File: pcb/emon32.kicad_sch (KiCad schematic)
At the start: 37 parts

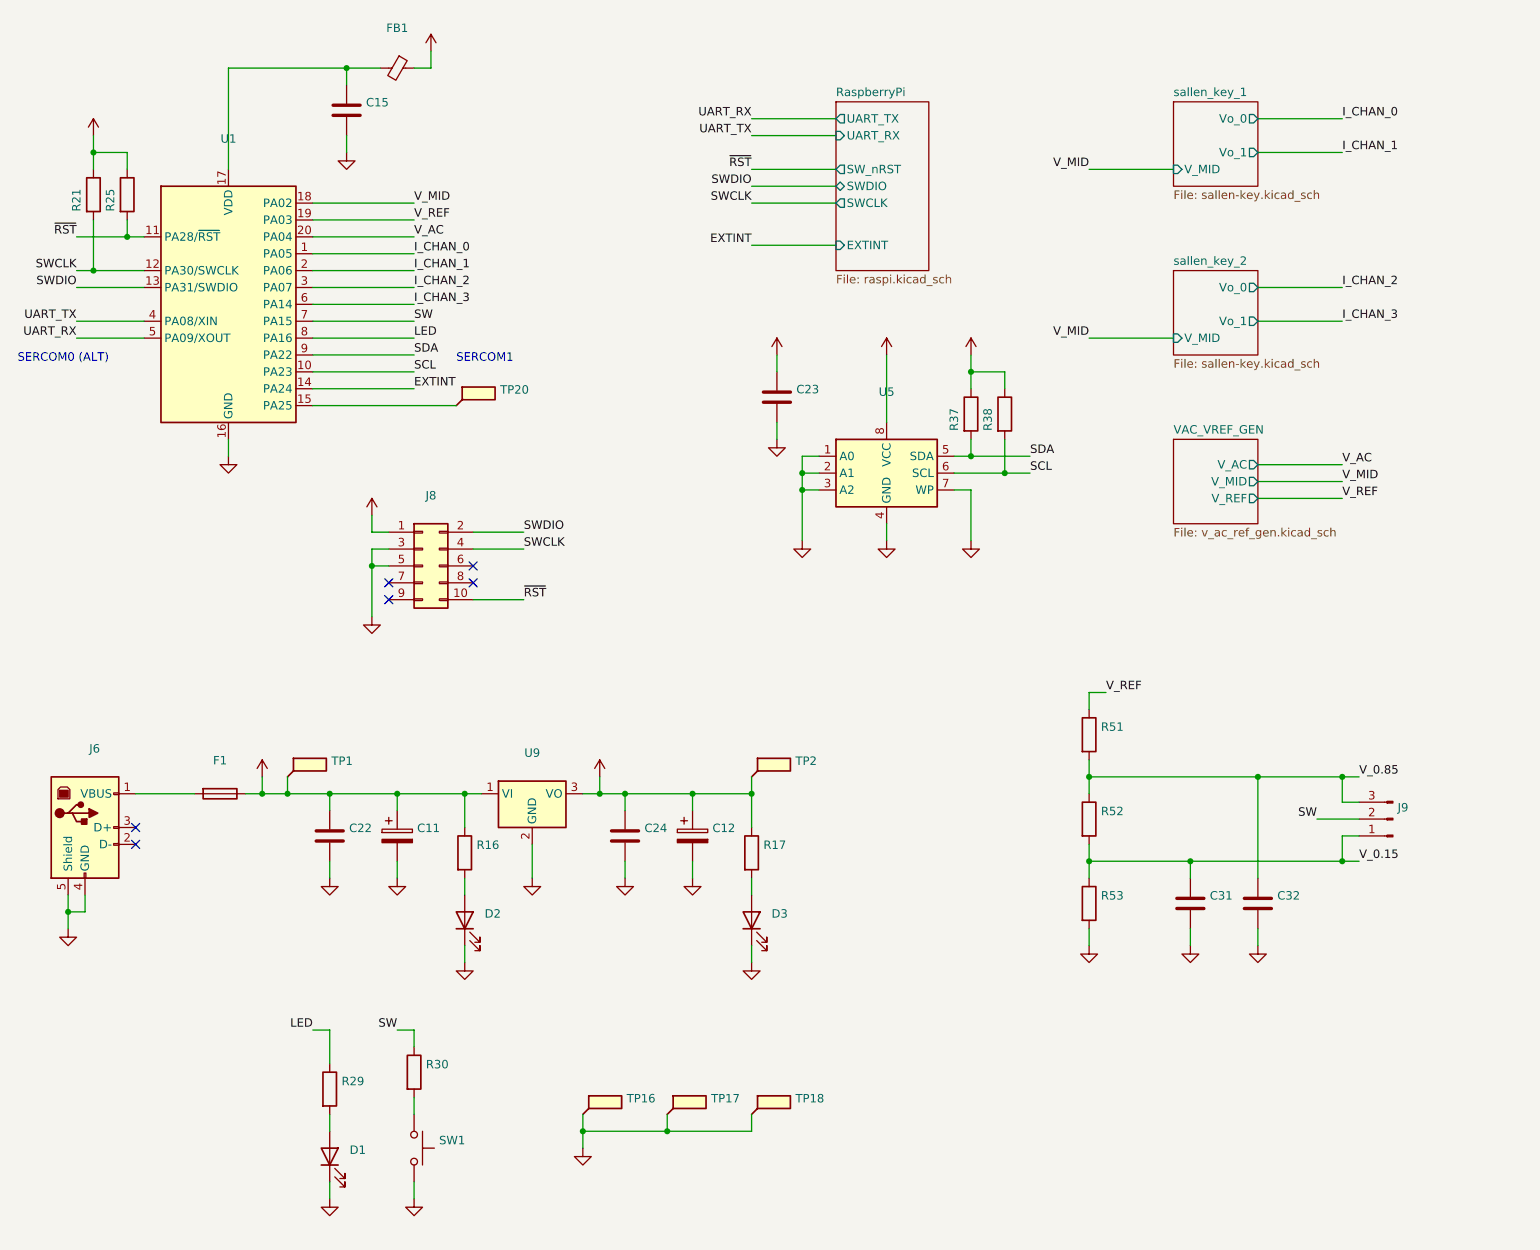
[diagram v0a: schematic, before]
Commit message: * Start replicating emonLibCM functionality
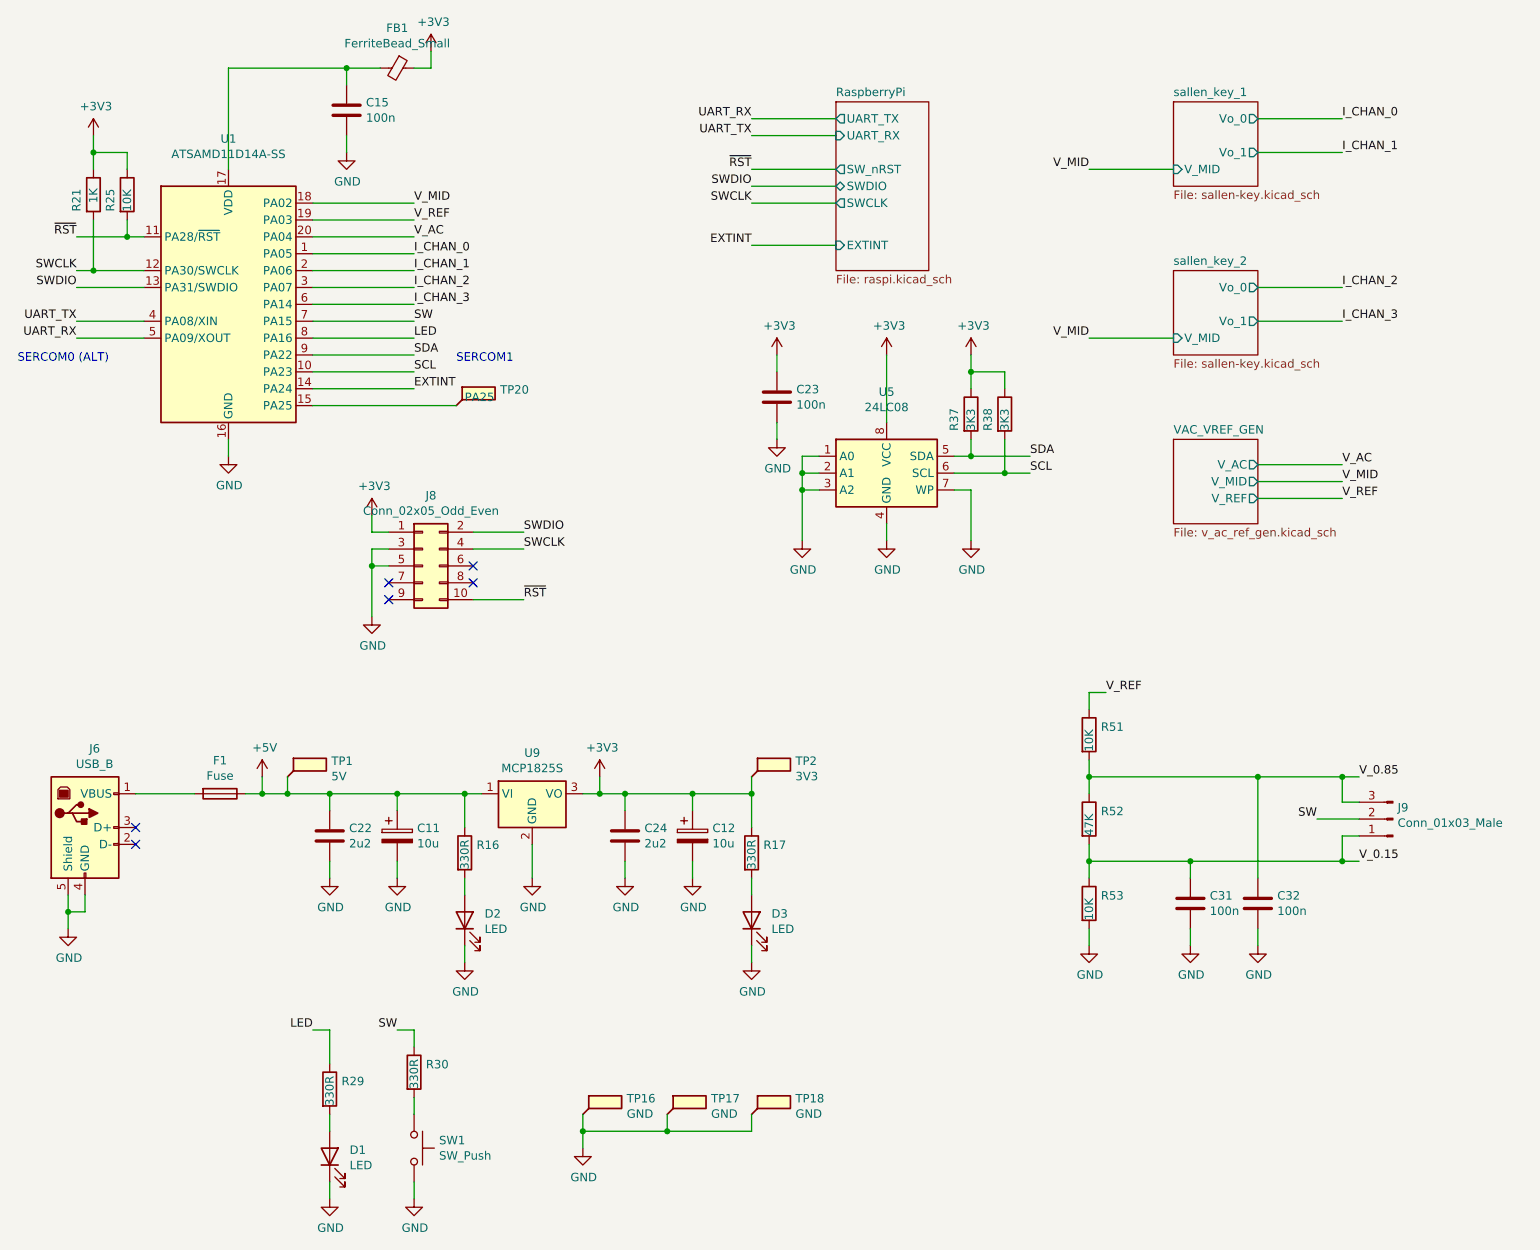
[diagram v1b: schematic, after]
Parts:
- C11, C12: value (none) -> 10u; footprint (none) -> Capacitor_THT:C_Radial_D6.3mm_H5.0mm_P2.50mm
- C15, C23, C31, C32: value (none) -> 100n; footprint (none) -> Capacitor_SMD:C_0805_2012Metric_Pad1.18x1.45mm_HandSolder
- C22, C24: value (none) -> 2u2; footprint (none) -> Capacitor_SMD:C_0805_2012Metric_Pad1.18x1.45mm_HandSolder
- D1, D2, D3: value (none) -> LED; footprint (none) -> LED_SMD:LED_0805_2012Metric_Pad1.15x1.40mm_HandSolder
- F1: value (none) -> Fuse; footprint (none) -> Fuse:Fuse_1206_3216Metric_Pad1.42x1.75mm_HandSolder
- FB1: value (none) -> FerriteBead_Small; footprint (none) -> Inductor_SMD:L_0805_2012Metric_Pad1.15x1.40mm_HandSolder
- J6: value (none) -> USB_B; footprint (none) -> Connector_USB:USB_Mini-B_Wuerth_65100516121_Horizontal
- J8: value (none) -> Conn_02x05_Odd_Even; footprint (none) -> Connector_PinHeader_1.27mm:PinHeader_2x05_P1.27mm_Vertical
- J9: value (none) -> Conn_01x03_Male; footprint (none) -> Connector_PinHeader_2.54mm:PinHeader_1x03_P2.54mm_Vertical
- R16, R17, R29, R30: value (none) -> 330R; footprint (none) -> Resistor_SMD:R_0805_2012Metric_Pad1.20x1.40mm_HandSolder
- R21: value (none) -> 1K; footprint (none) -> Resistor_SMD:R_0805_2012Metric_Pad1.20x1.40mm_HandSolder
- R25, R51, R53: value (none) -> 10K; footprint (none) -> Resistor_SMD:R_0805_2012Metric_Pad1.20x1.40mm_HandSolder
- R37, R38: value (none) -> 3K3; footprint (none) -> Resistor_SMD:R_0805_2012Metric_Pad1.20x1.40mm_HandSolder
- R52: value (none) -> 47K; footprint (none) -> Resistor_SMD:R_0805_2012Metric_Pad1.20x1.40mm_HandSolder
- SW1: value (none) -> SW_Push; footprint (none) -> Button_Switch_THT:SW_PUSH_6mm
- TP1: value (none) -> 5V; footprint (none) -> TestPoint:TestPoint_THTPad_1.5x1.5mm_Drill0.7mm
- TP16, TP17, TP18: value (none) -> GND; footprint (none) -> TestPoint:TestPoint_THTPad_1.5x1.5mm_Drill0.7mm
- TP2: value (none) -> 3V3; footprint (none) -> TestPoint:TestPoint_THTPad_1.5x1.5mm_Drill0.7mm
- TP20: value (none) -> PA25; footprint (none) -> TestPoint:TestPoint_THTPad_1.5x1.5mm_Drill0.7mm
- U1: value (none) -> ATSAMD11D14A-SS; footprint (none) -> Package_SO:SOIC-20W_7.5x12.8mm_P1.27mm
- U5: value (none) -> 24LC08; footprint (none) -> Package_SO:SOIC-8_3.9x4.9mm_P1.27mm
- U9: value (none) -> MCP1825S; footprint (none) -> Package_TO_SOT_SMD:SOT-223
